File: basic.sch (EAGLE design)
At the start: 27 parts, among them U1 RASPBERRY_PICOTH

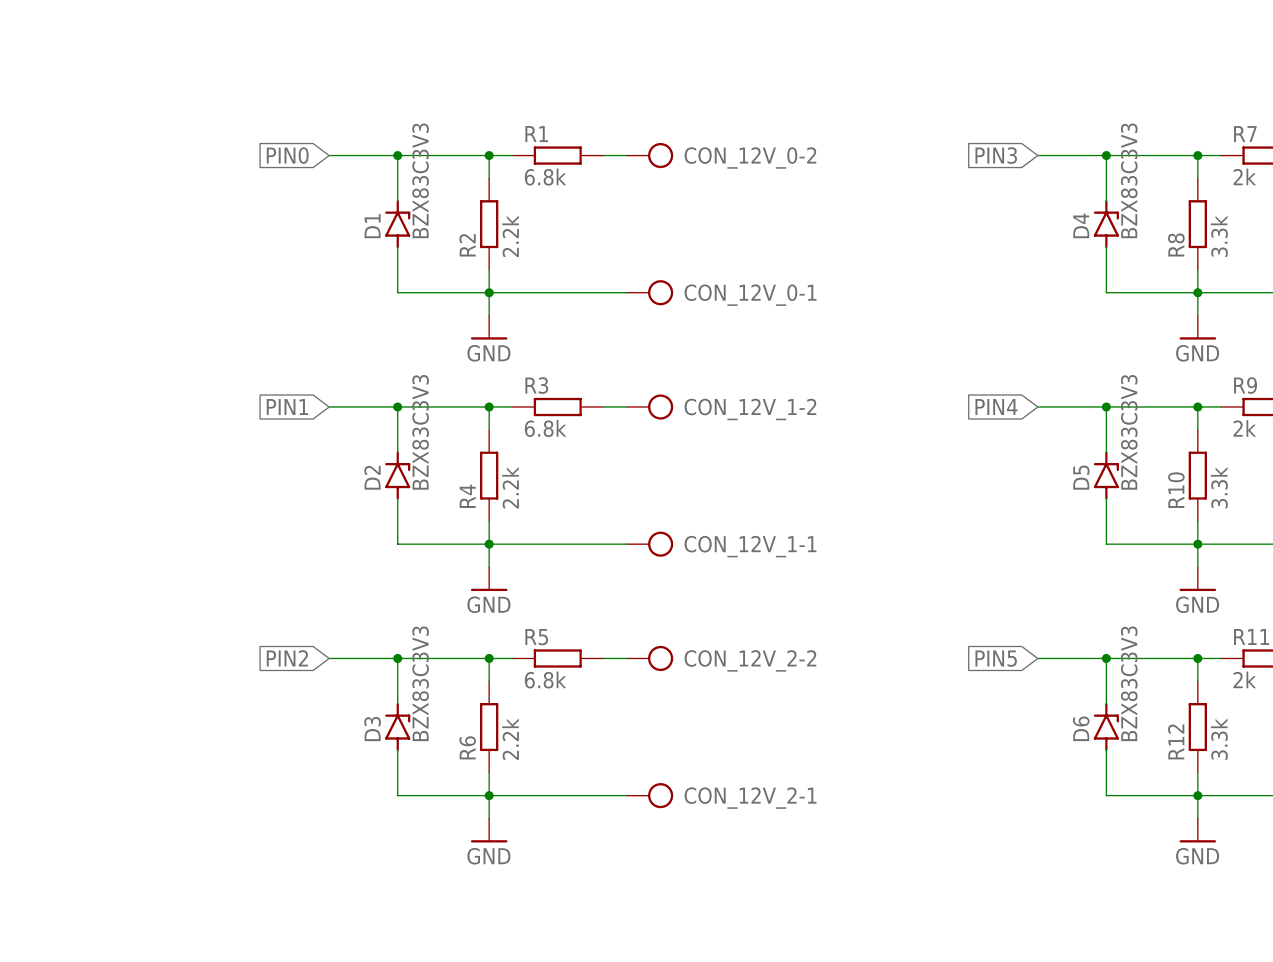
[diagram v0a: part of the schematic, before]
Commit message: Added capacitors to catch voltage spikes
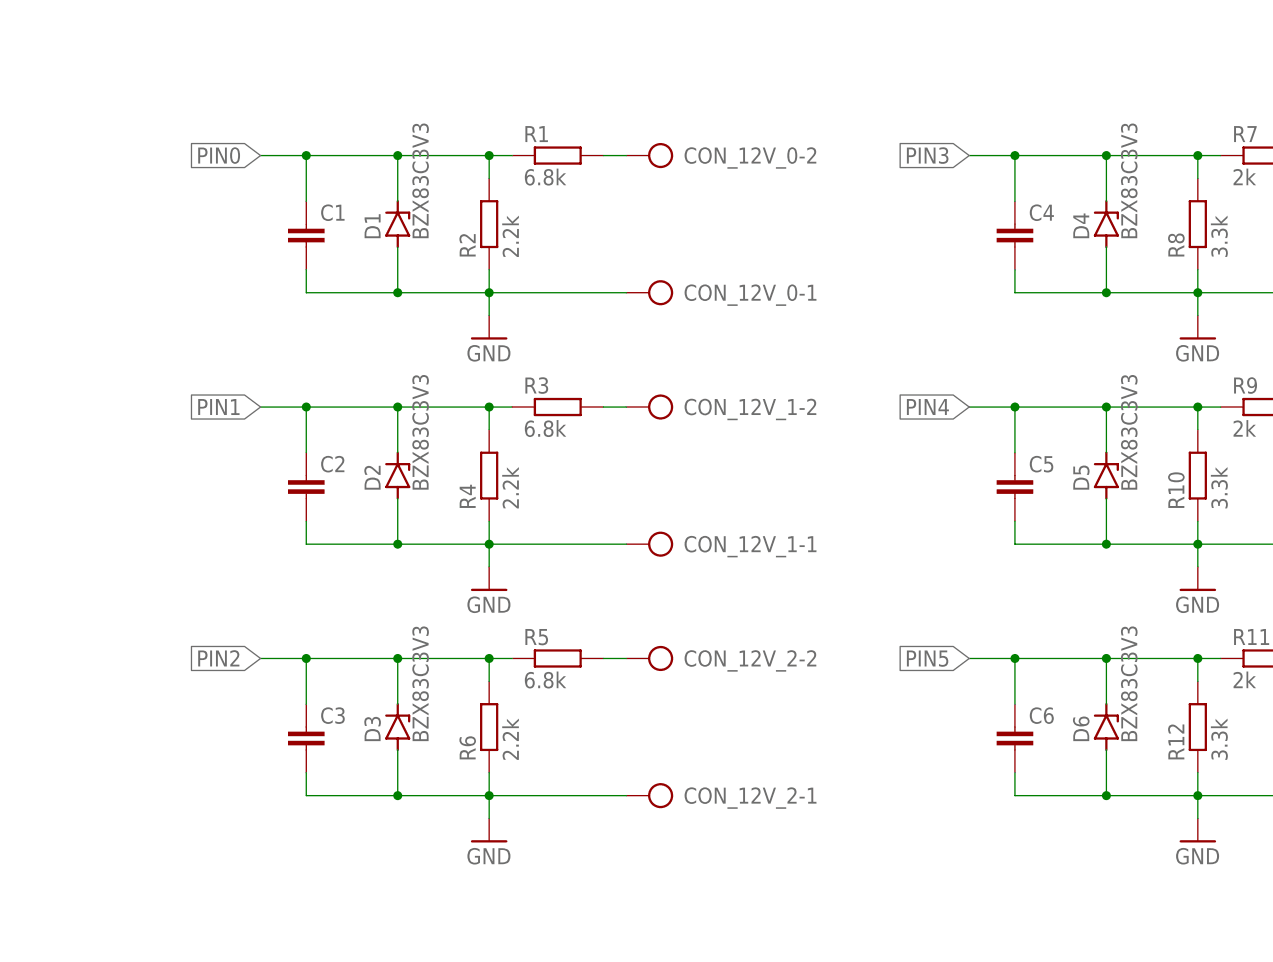
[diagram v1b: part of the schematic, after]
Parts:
- added C1, C2, C3, C4, C5, C6: (no value), rcl:C-EU025-050X050
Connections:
- net GND: now also C1.2, C2.2, C3.2, C4.2, C5.2, C6.2
- net PIN0: now also C1.1
- net PIN1: now also C2.1
- net PIN2: now also C3.1
- net PIN3: now also C4.1
- net PIN4: now also C5.1
- net PIN5: now also C6.1
